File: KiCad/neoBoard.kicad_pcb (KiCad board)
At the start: 2 copper layers, 40 x 40 mm, 74 parts, among them J1 SW, J10 CONN_01X04_Straight, J11 CONN_01X04_Straight, J12 CONN_01X04_Straight, J13 CONN_01X04_Straight, J2 μUSB, J3 BATT, J6 CONN_01X12_Straight, J7 CONN_02X12_Straight, J8 CONN_01X04_Straight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

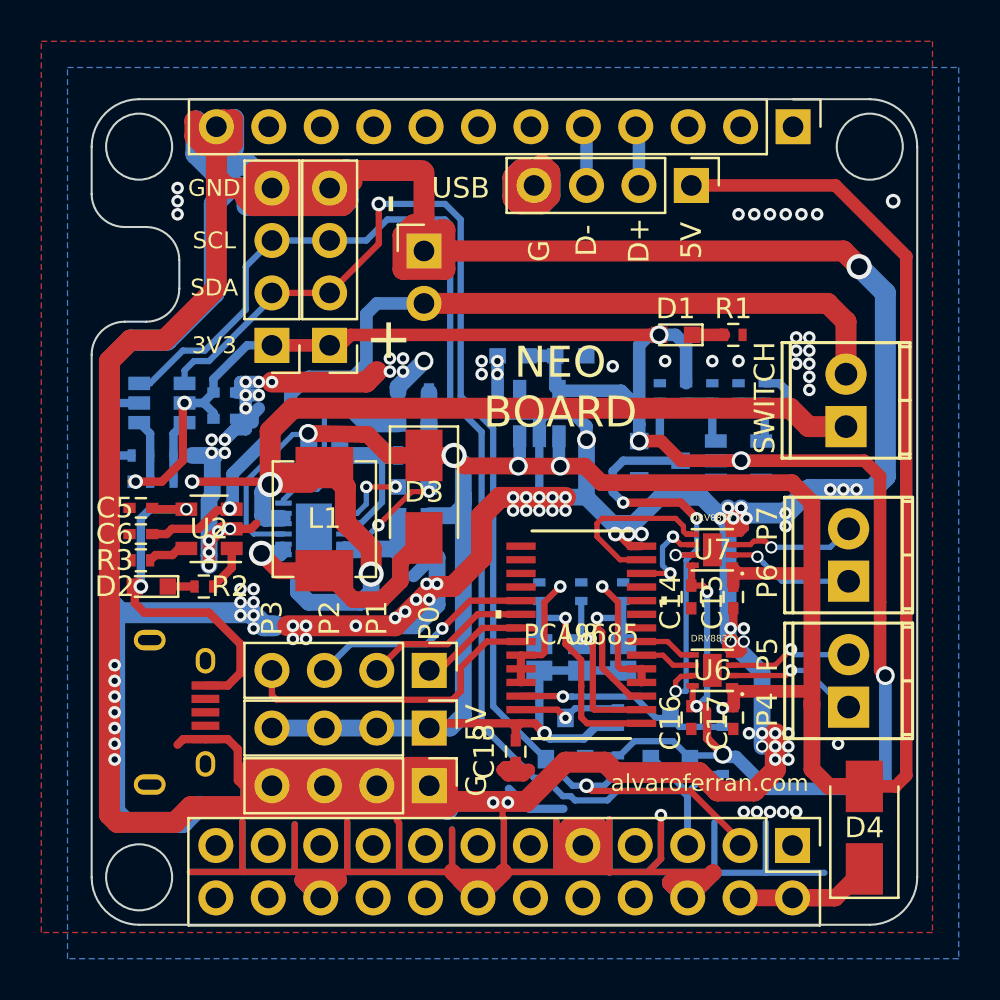
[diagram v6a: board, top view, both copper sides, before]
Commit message: Improved GND connections
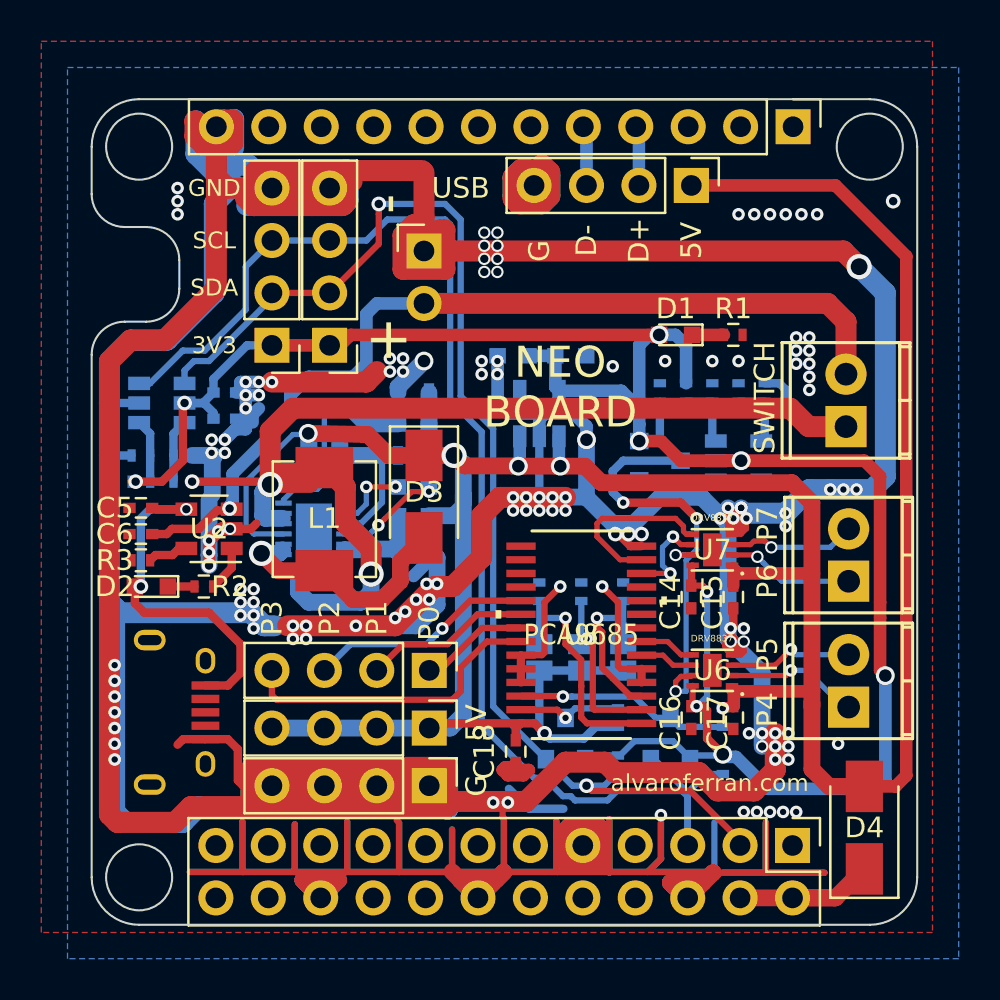
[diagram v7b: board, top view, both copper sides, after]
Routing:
- net GND: track 575.0 -> 582.9 mm, vias 121 -> 129
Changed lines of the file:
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@@
     (thickness 1.6)
     (drawings 69)
-    (tracks 1039)
+    (tracks 1050)
     (zones 0)
     (modules 74)
@@
   )
   (setup
-    (last_trace_width 0.6096)
+    (last_trace_width 0.25)
     (user_trace_width 0.1524)
     (user_trace_width 0.254)
@@
   (gr_line (start 151.137578 71.229122) (end 150.090325 71.229122) (layer Edge.Cuts) (width 0.1))
   (gr_line (start 148.490325 69.629122) (end 148.490325 67.335634) (layer Edge.Cuts) (width 0.1))
+  (segment (start 178.5874 102.5144) (end 181.1528 102.5144) (width 0.3048) (layer F.Cu) (net 40))
+  (segment (start 181.1528 102.5144) (end 183.9976 102.5144) (width 0.3048) (layer F.Cu) (net 40))
+  (segment (start 181.1528 102.5144) (end 181.1528 100.076) (width 0.3048) (layer F.Cu) (net 40))
+  (via (at 168.148 72.136) (size 0.6) (drill 0.4) (layers F.Cu B.Cu) (net 40))
+  (via (at 168.148 72.771) (size 0.6) (drill 0.4) (layers F.Cu B.Cu) (net 40))
+  (via (at 167.513 72.771) (size 0.6) (drill 0.4) (layers F.Cu B.Cu) (net 40))
+  (via (at 168.148 71.501) (size 0.6) (drill 0.4) (layers F.Cu B.Cu) (net 40))
+  (via (at 167.513 72.136) (size 0.6) (drill 0.4) (layers F.Cu B.Cu) (net 40))
+  (via (at 168.148 73.406) (size 0.6) (drill 0.4) (layers F.Cu B.Cu) (net 40))
+  (via (at 167.513 71.501) (size 0.6) (drill 0.4) (layers F.Cu B.Cu) (net 40))
+  (via (at 167.513 73.406) (size 0.6) (drill 0.4) (layers F.Cu B.Cu) (net 40))
   (via (at 154.178 86.995) (size 0.6096) (drill 0.3048) (layers F.Cu B.Cu) (net 40))
   (via (at 154.178 86.4235) (size 0.6096) (drill 0.3048) (layers F.Cu B.Cu) (net 40))

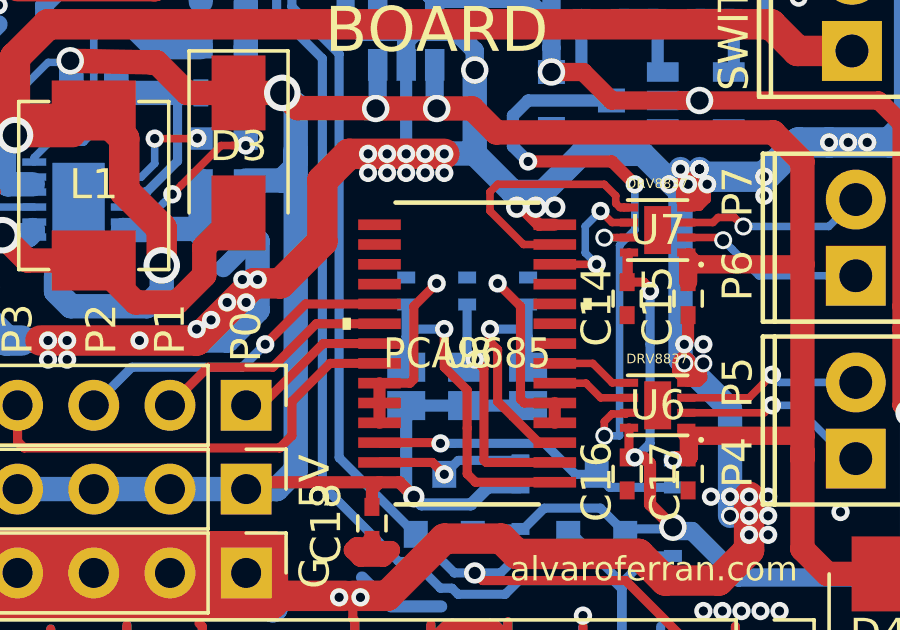
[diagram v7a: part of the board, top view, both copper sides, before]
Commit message: Improved GND connections
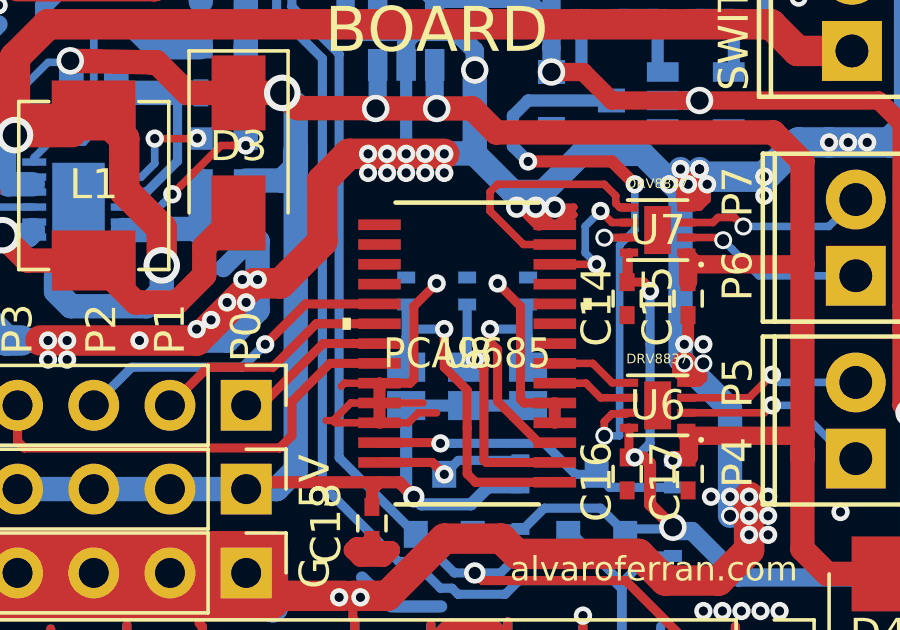
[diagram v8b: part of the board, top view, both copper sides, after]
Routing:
- net GND: track 582.9 -> 595.1 mm
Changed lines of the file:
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@@
     (thickness 1.6)
     (drawings 69)
-    (tracks 1050)
+    (tracks 1072)
     (zones 0)
     (modules 74)
@@
     (34 B.Paste user hide)
     (35 F.Paste user hide)
-    (36 B.SilkS user)
+    (36 B.SilkS user hide)
     (37 F.SilkS user)
     (38 B.Mask user hide)
@@
     (pad_to_mask_clearance 0.2)
     (aux_axis_origin 0 0)
-    (visible_elements FFF9BE1F)
+    (visible_elements FFF9BA1F)
     (pcbplotparams
       (layerselection 0x01030_ffffffff)
@@
   (gr_line (start 151.137578 71.229122) (end 150.090325 71.229122) (layer Edge.Cuts) (width 0.1))
   (gr_line (start 148.490325 69.629122) (end 148.490325 67.335634) (layer Edge.Cuts) (width 0.1))
+  (segment (start 174.8282 86.6902) (end 174.625 86.487) (width 0.25) (layer F.Cu) (net 40))
+  (segment (start 175.133 86.6902) (end 174.8282 86.6902) (width 0.25) (layer F.Cu) (net 40))
+  (segment (start 175.133 86.6902) (end 174.5996 86.6902) (width 0.25) (layer F.Cu) (net 40))
+  (segment (start 175.1838 86.6902) (end 175.133 86.6902) (width 0.25) (layer F.Cu) (net 40))
+  (segment (start 175.1838 86.6902) (end 175.387 86.487) (width 0.25) (layer F.Cu) (net 40))
+  (segment (start 175.133 86.6902) (end 175.4378 86.6902) (width 0.25) (layer F.Cu) (net 40))
+  (segment (start 175.4378 86.6902) (end 175.768 86.36) (width 0.25) (layer F.Cu) (net 40))
+  (segment (start 175.768 86.36) (end 175.514 86.36) (width 0.25) (layer F.Cu) (net 40))
+  (segment (start 175.514 86.36) (end 175.768 86.106) (width 0.25) (layer F.Cu) (net 40))
+  (segment (start 175.768 86.106) (end 175.133 86.106) (width 0.25) (layer F.Cu) (net 40))
+  (segment (start 175.133 86.6902) (end 175.0822 86.6902) (width 0.25) (layer F.Cu) (net 40))
+  (segment (start 175.0822 86.6902) (end 174.498 86.106) (width 0.25) (layer F.Cu) (net 40))
+  (segment (start 168.1226 91.9734) (end 168.021 92.075) (width 0.25) (layer F.Cu) (net 40))
+  (segment (start 169.291 91.9734) (end 168.1226 91.9734) (width 0.25) (layer F.Cu) (net 40))
+  (segment (start 169.291 93.2942) (end 167.8218 93.2942) (width 0.25) (layer F.Cu) (net 40))
+  (segment (start 167.8218 93.2942) (end 167.7456 93.218) (width 0.25) (layer F.Cu) (net 40))
+  (segment (start 170.5824 92.964) (end 171.196 92.964) (width 0.25) (layer F.Cu) (net 40))
+  (segment (start 169.291 93.2942) (end 170.2522 93.2942) (width 0.25) (layer F.Cu) (net 40))
+  (segment (start 170.2522 93.2942) (end 170.5824 92.964) (width 0.25) (layer F.Cu) (net 40))
+  (segment (start 169.291 92.6338) (end 170.7388 92.6338) (width 0.25) (layer F.Cu) (net 40))
+  (segment (start 167.7456 93.218) (end 167.513 93.218) (width 0.25) (layer F.Cu) (net 40))
+  (segment (start 169.291 92.6338) (end 168.3298 92.6338) (width 0.25) (layer F.Cu) (net 40))
+  (segment (start 168.3298 92.6338) (end 167.7456 93.218) (width 0.25) (layer F.Cu) (net 40))
   (segment (start 178.5874 102.5144) (end 181.1528 102.5144) (width 0.3048) (layer F.Cu) (net 40))
   (segment (start 181.1528 102.5144) (end 183.9976 102.5144) (width 0.3048) (layer F.Cu) (net 40))
@@
   (segment (start 174.0154 86.106) (end 173.863 86.106) (width 0.4064) (layer F.Cu) (net 40))
   (segment (start 174.5996 86.6902) (end 174.0154 86.106) (width 0.4064) (layer F.Cu) (net 40))
-  (segment (start 175.133 86.6902) (end 174.5996 86.6902) (width 0.4064) (layer F.Cu) (net 40))
   (via (at 173.863 86.106) (size 0.7112) (drill 0.4064) (layers F.Cu B.Cu) (net 40))
   (segment (start 178.054 84.328) (end 179.324 85.598) (width 0.8128) (layer B.Cu) (net 40))
